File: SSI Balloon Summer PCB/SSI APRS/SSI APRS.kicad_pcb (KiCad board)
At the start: 4 copper layers, 80 x 45 mm, 35 parts, among them J1 Conn_01x08, J4 APRS antenna, M1 MountingHole_3.2mm_M3, M2 MountingHole_3.2mm_M3, M3 MountingHole_3.2mm_M3, M4 MountingHole_3.2mm_M3, U12 TPS63070RNMR, U5 DRA818V

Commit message: APRS naming convention stuff
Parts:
- renumbered TP7 to +4V1, TP4 to +5V, TP3 to APRS_AUDIO, TP2 to APRS_PD, TP1 to APRS_PTT, TP6 to GND, TP5 to GND
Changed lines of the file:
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@@
 		(descr "Through hole straight pin header, 1x01, 2.54mm pitch, single row")
 		(tags "Through hole pin header THT 1x01 2.54mm single row")
-		(property "Reference" "TP2"
+		(property "Reference" "APRS_PD"
 			(at 0 -2.38 0)
 			(layer "F.SilkS")
@@
 		(descr "Through hole straight pin header, 1x01, 2.54mm pitch, single row")
 		(tags "Through hole pin header THT 1x01 2.54mm single row")
-		(property "Reference" "TP6"
+		(property "Reference" "GND"
 			(at 0 -3 0)
 			(layer "F.SilkS")
@@
 		(descr "Through hole straight pin header, 1x01, 2.54mm pitch, single row")
 		(tags "Through hole pin header THT 1x01 2.54mm single row")
-		(property "Reference" "TP3"
+		(property "Reference" "APRS_AUDIO"
 			(at 0 -2.38 0)
 			(layer "F.SilkS")
@@
 		(descr "Through hole straight pin header, 1x01, 2.54mm pitch, single row")
 		(tags "Through hole pin header THT 1x01 2.54mm single row")
-		(property "Reference" "TP5"
+		(property "Reference" "GND"
 			(at 0 -3 0)
 			(layer "F.SilkS")
@@
 		(descr "Through hole straight pin header, 1x01, 2.54mm pitch, single row")
 		(tags "Through hole pin header THT 1x01 2.54mm single row")
-		(property "Reference" "TP1"
+		(property "Reference" "APRS_PTT"
 			(at 0 -2.38 0)
 			(layer "F.SilkS")
@@
 		(descr "Through hole straight pin header, 1x01, 2.54mm pitch, single row")
 		(tags "Through hole pin header THT 1x01 2.54mm single row")
-		(property "Reference" "TP7"
+		(property "Reference" "+4V1"
 			(at 0 -3 0)
 			(layer "F.SilkS")
@@
 		(descr "Through hole straight pin header, 1x01, 2.54mm pitch, single row")
 		(tags "Through hole pin header THT 1x01 2.54mm single row")
-		(property "Reference" "TP4"
+		(property "Reference" "+5V"
 			(at 0 -3 0)
 			(layer "F.SilkS")
@@
 	)
 	(segment
-		(start 171.425 118.84)
-		(end 169.7 118.84)
+		(start 136.5 97)
+		(end 148.775 97)
 		(width 0.2)
 		(layer "F.Cu")
-		(net "Net-(C36-Pad2)")
+		(net "/APRS_PD")
 	)
 	(segment
-		(start 165.175 118.84)
-		(end 165.025 118.69)
+		(start 146.975 96.84)
+		(end 147.375 96.44)
 		(width 0.2)
 		(layer "F.Cu")
-		(net "Net-(U5-MIC_IN)")
+		(net "/APRS_PD")
 	)
 	(segment
-		(start 170.025 116.99)
-		(end 170.2 117.165)
+		(start 136.5 95)
+		(end 136.5 97)
 		(width 0.2)
 		(layer "F.Cu")
-		(net "Net-(U5-MIC_IN)")
+		(net "/APRS_PD")
 	)
 	(segment
-		(start 168.2 116.99)
-		(end 170.025 116.99)
+		(start 128.5 94.5)
+		(end 131 97)
 		(width 0.2)
 		(layer "F.Cu")
-		(net "Net-(U5-MIC_IN)")
+		(net "/APRS_PD")
 	)
 	(segment
-		(start 168.05 118.84)
-		(end 168.05 117.315)
+		(start 131 97)
+		(end 136.5 97)
 		(width 0.2)
 		(layer "F.Cu")
-		(net "Net-(U5-MIC_IN)")
+		(net "/APRS_PD")
 	)
 	(segment
-		(start 168.05 117.315)
-		(end 168.2 117.165)
+		(start 171.425 118.84)
+		(end 169.7 118.84)
 		(width 0.2)
 		(layer "F.Cu")
-		(net "Net-(U5-MIC_IN)")
+		(net "Net-(C36-Pad2)")
 	)
 	(segment
-		(start 168.05 118.84)
-		(end 165.175 118.84)
+		(start 165.175 118.84)
+		(end 165.025 118.69)
 		(width 0.2)
 		(layer "F.Cu")
@@
 	)
 	(segment
-		(start 136.5 97)
-		(end 148.775 97)
+		(start 170.025 116.99)
+		(end 170.2 117.165)
 		(width 0.2)
 		(layer "F.Cu")
-		(net "/APRS_PD")
+		(net "Net-(U5-MIC_IN)")
 	)
 	(segment
-		(start 146.975 96.84)
-		(end 147.375 96.44)
+		(start 168.2 116.99)
+		(end 170.025 116.99)
 		(width 0.2)
 		(layer "F.Cu")
-		(net "/APRS_PD")
+		(net "Net-(U5-MIC_IN)")
 	)
 	(segment
-		(start 136.5 95)
-		(end 136.5 97)
+		(start 168.05 118.84)
+		(end 168.05 117.315)
 		(width 0.2)
 		(layer "F.Cu")
-		(net "/APRS_PD")
+		(net "Net-(U5-MIC_IN)")
 	)
 	(segment
-		(start 128.5 94.5)
-		(end 131 97)
+		(start 168.05 117.315)
+		(end 168.2 117.165)
 		(width 0.2)
 		(layer "F.Cu")
-		(net "/APRS_PD")
+		(net "Net-(U5-MIC_IN)")
 	)
 	(segment
-		(start 131 97)
-		(end 136.5 97)
+		(start 168.05 118.84)
+		(end 165.175 118.84)
 		(width 0.2)
 		(layer "F.Cu")
-		(net "/APRS_PD")
+		(net "Net-(U5-MIC_IN)")
 	)
 	(segment

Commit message: Updated antenna connector
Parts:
- J4: footprint Connector_Coaxial:U.FL_Hirose_U.FL-R-SMT-1_Vertical -> Connector_Coaxial:SMA_Amphenol_901-144_Vertical; moved to B.Cu
- moved M2 5.00 mm to (181.0, 86.5)
- moved M4 4.50 mm to (181.0, 123.5)
- moved J4 1.26 mm to (172.0, 91.8), turned to 180 degrees
- renumbered APRS_PTT to TP1, APRS_PD to TP2, APRS_AUDIO to TP3, +5V to TP4, GND to TP5, GND to TP6, +4V1 to TP7
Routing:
- net GND: track 50.0 -> 54.7 mm, vias 29 -> 31
- net Net-(J4-In): track 4.21 -> 7.00 mm
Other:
- board size 80 x 45 mm -> 84.5 x 45 mm

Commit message: PCB finally done i think and ready to order
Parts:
- C19: value 100 nF -> 100nF
- R10: value 100k -> 120k
- R9: value 412k -> 510k
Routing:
- net GND: track 54.7 -> 61.5 mm, vias 31 -> 36
- net /APRS_PD: track 23.9 -> 22.7 mm
- net Net-(U12-EN): track 7.04 -> 6.21 mm

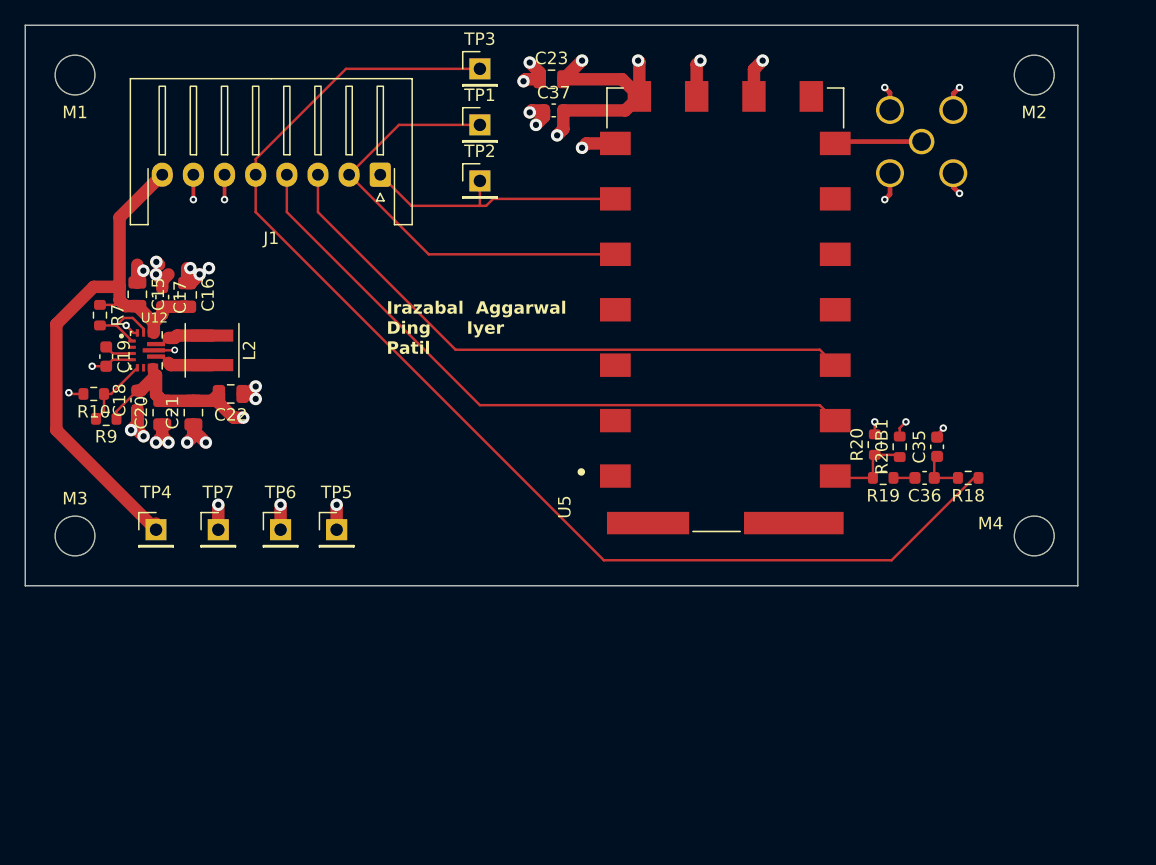
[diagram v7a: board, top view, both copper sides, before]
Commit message: Board done but we have a price crisis so might have to change things
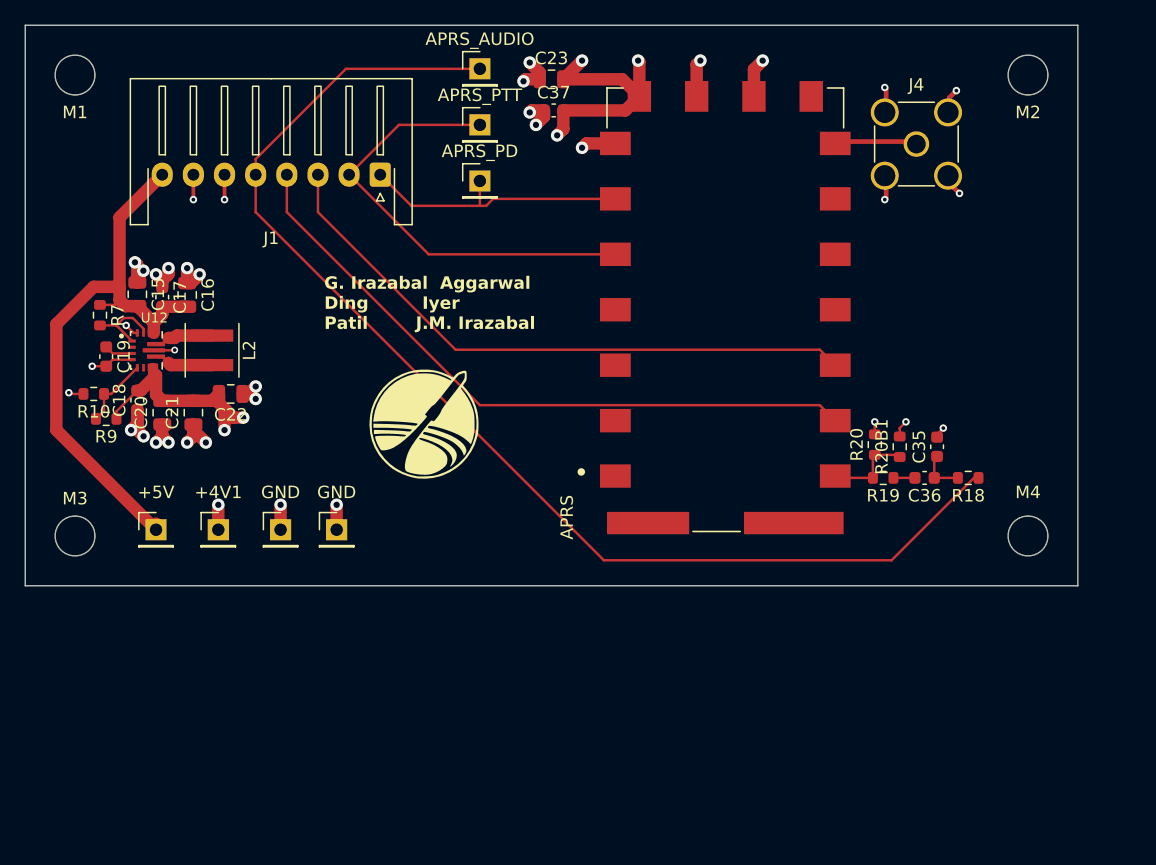
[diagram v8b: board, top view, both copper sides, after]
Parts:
- added G***: LOGO, LOGO, F.Cu at (132.0, 114.5)
- J4: moved to F.Cu
- moved M2 0.50 mm to (180.5, 86.5)
- moved M4 0.50 mm to (180.5, 123.5)
- moved J4 0.47 mm to (171.5, 92.0), turned to 0 degrees
- renumbered TP7 to +4V1, TP4 to +5V, U5 to APRS, TP3 to APRS_AUDIO, TP2 to APRS_PD, TP1 to APRS_PTT, TP6 to GND, TP5 to GND
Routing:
- net GND: track 61.5 -> 63.9 mm
- net +4V1: track 38.4 -> 40.0 mm, vias 5 -> 6
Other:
- board text added: "G. Irazabal Aggarwal Ding Iyer Patil J.M. Irazabal"
- board text removed: "Irazabal Aggarwal Ding Iyer Patil"
